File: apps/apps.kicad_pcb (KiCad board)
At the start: 2 copper layers, 25 x 25 mm, 14 parts, among them J1 Conn_OUTPUT, Q1 SS9013, U1 XTR117

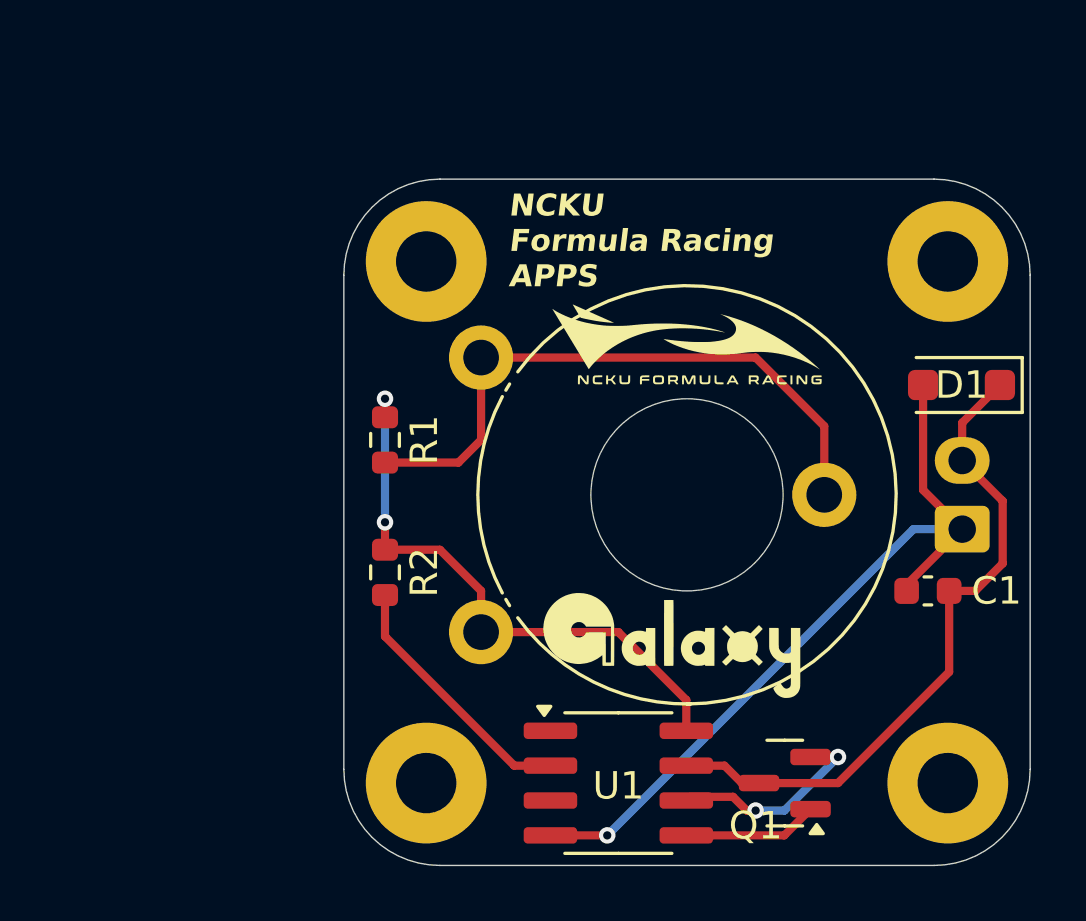
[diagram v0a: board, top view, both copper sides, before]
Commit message: chore: change XTR117 footprint
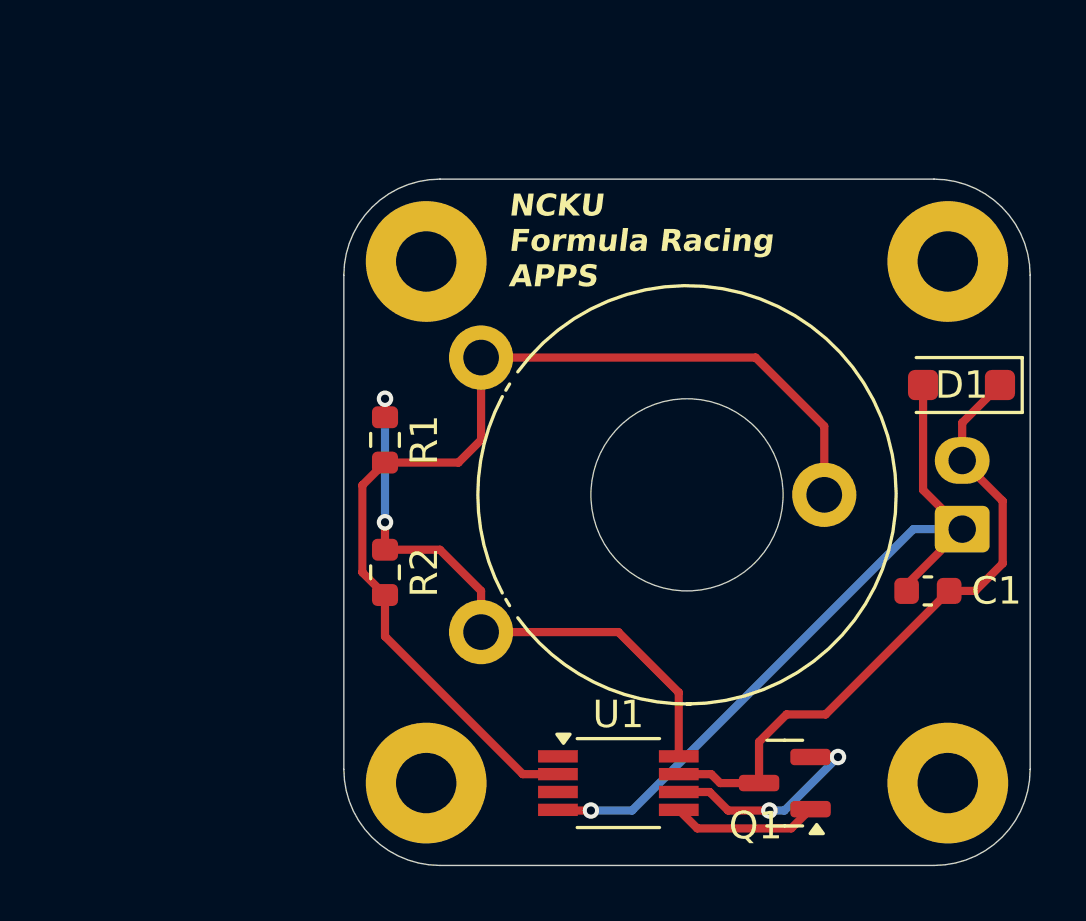
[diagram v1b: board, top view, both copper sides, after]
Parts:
- G*** (x2): moved to B.Cu
- R1: value 83k -> 45k
- RV1: value PT15LV02-253 -> PT15GV02-104
- U1: footprint Package_SO:SOIC-8_3.9x4.9mm_P1.27mm -> Package_SO:VSSOP-8_3.0x3.0mm_P0.65mm
- moved G*** 11.0 mm to (101.5, 53.5), turned to 180 degrees
- moved G*** 4.00 mm to (101.5, 49.5), turned to 180 degrees
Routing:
- net Net-(U1-IIN): track 32.4 -> 38.3 mm
- net Net-(U1-VREG): track 21.4 -> 22.2 mm
- net VDC: track 24.5 -> 23.8 mm
- net Net-(D1-A): track 28.5 -> 27.9 mm
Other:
- board text added: "R=3.5"

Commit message: feat: implement apps pcb
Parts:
- moved D1 11.4 mm to (101.0, 50.5)
- moved G*** 11.4 mm to (91.0, 45.0)
- moved G*** 11.4 mm to (91.0, 49.0)
- moved H1 11.4 mm to (100.5, 46.0)
- moved H2 11.4 mm to (100.5, 65.0)
- moved H3 11.4 mm to (81.5, 65.0)
- moved H4 11.4 mm to (81.5, 46.0)
- moved Q1 11.4 mm to (94.6, 65.0)
- moved R1 11.4 mm to (80.0, 52.5)
- moved R2 11.4 mm to (80.0, 57.3)
- moved U1 11.4 mm to (88.5, 65.0)
- moved J1 11.2 mm to (100.9, 56.8)
- moved RV1 11.1 mm to (83.5, 60.5)
- moved C1 10.5 mm to (99.9, 61.1)
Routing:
- net Net-(Q1-B): track 7.89 -> 10.4 mm
- net Net-(U1-IIN): track 38.3 -> 36.0 mm, vias 0 -> 2
- net Net-(D1-A): track 27.9 -> 26.8 mm, vias 1 -> 0
- net VDC: track 23.8 -> 24.5 mm
- net Net-(U1-VREG): track 22.2 -> 22.8 mm
- net Net-(Q1-E): track 5.37 -> 4.81 mm

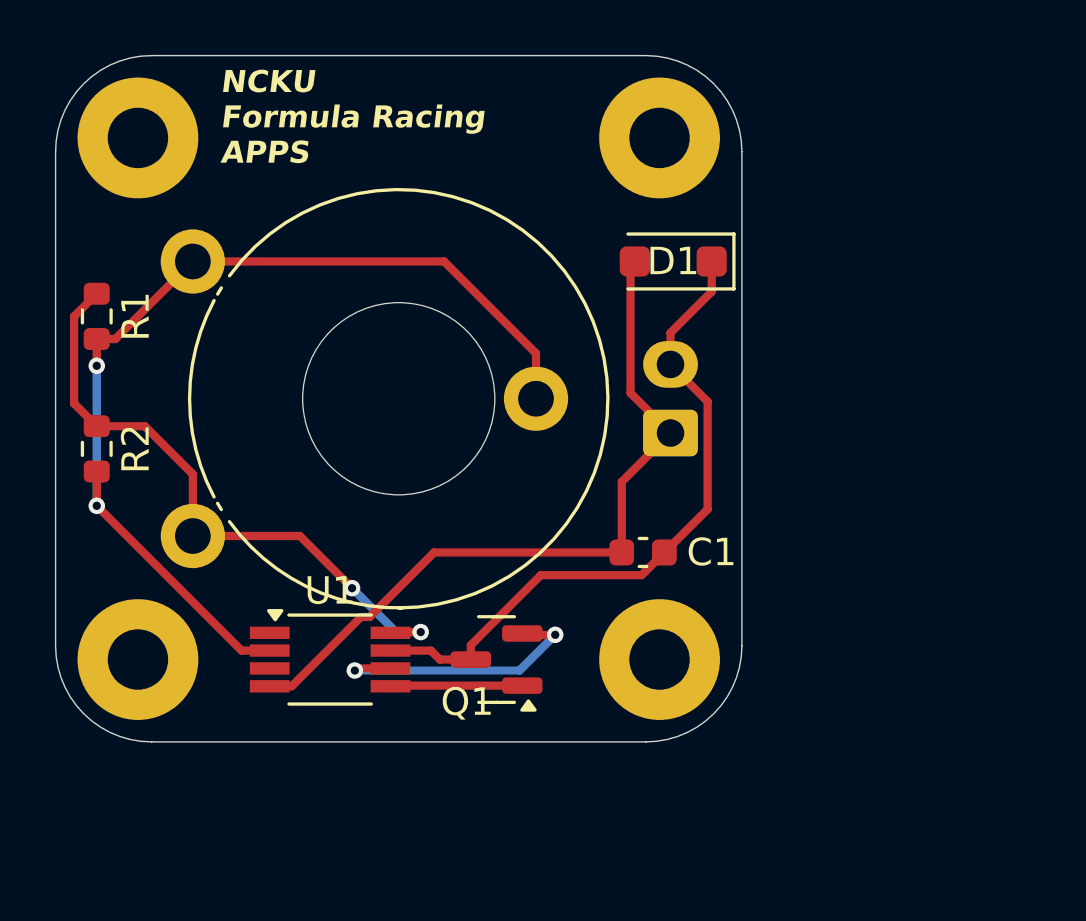
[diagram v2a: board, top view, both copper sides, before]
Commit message: fix: update resistor
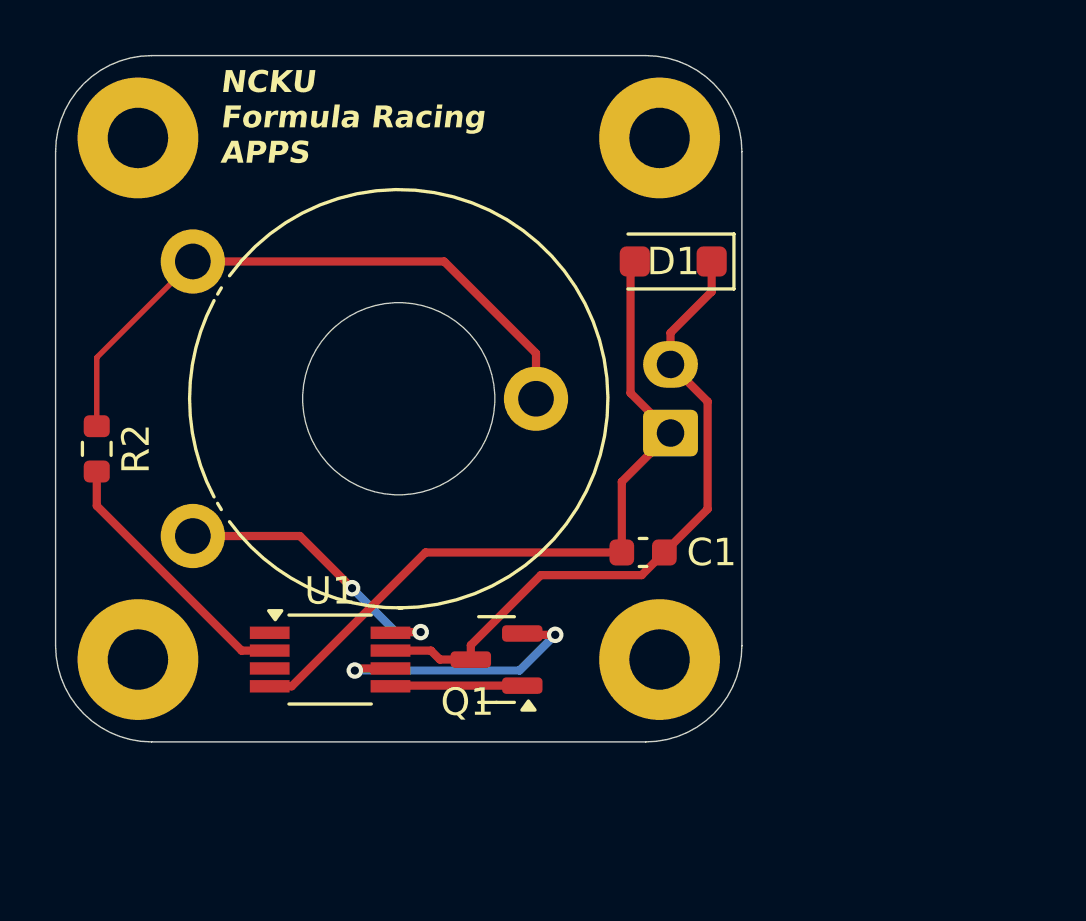
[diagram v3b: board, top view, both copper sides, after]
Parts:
- removed R1: 45k, Resistor_SMD:R_0603_1608Metric
- R2: value 125k -> 25k
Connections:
- R2 pad 1: Net-(U1-VREG) -> Net-(R2-Pad1)
- RV1 pad 2: Net-(U1-IIN) -> Net-(R2-Pad1)
- RV1 pad 3: Net-(U1-IIN) -> Net-(R2-Pad1)
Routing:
- net Net-(U1-IIN): track 36.0 -> 9.73 mm, vias 2 -> 0
- net Net-(R2-Pad1): track 0.00 -> 23.0 mm
- net Net-(U1-VREG): track 22.8 -> 10.9 mm

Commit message: update the version of APPS
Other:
- board text added: "APPS 4mA~20mA Output Rev. 2026.02"
- board text removed: "APPS 4mA~20mA Output Rev. 2025.03"
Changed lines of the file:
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@@
 			(outputformat 1)
 			(mirror no)
-			(drillshape 1)
+			(drillshape 0)
 			(scaleselection 1)
-			(outputdirectory "")
+			(outputdirectory "C:/Users/kevin/Desktop/0225_output/APPS/")
 		)
 	)
@@
 			(size 4.4 4.4)
 			(drill 2.2)
-			(layers "*.Cu" "*.Mask")
+			(layers "*.Cu" "*.Mask" "In1.Cu" "In2.Cu" "In3.Cu" "In4.Cu" "In5.Cu" "In6.Cu"
+				"In7.Cu" "In8.Cu" "In9.Cu" "In10.Cu" "In11.Cu" "In12.Cu" "In13.Cu" "In14.Cu"
+				"In15.Cu" "In16.Cu" "In17.Cu" "In18.Cu" "In19.Cu" "In20.Cu" "In21.Cu"
+				"In22.Cu" "In23.Cu" "In24.Cu" "In25.Cu" "In26.Cu" "In27.Cu" "In28.Cu"
+				"In29.Cu" "In30.Cu"
+			)
 			(remove_unused_layers no)
 			(net 9 "unconnected-(H1-Pad1)")
@@
 			(size 7 7)
 			(drill 7)
-			(layers "*.Cu" "*.Mask")
+			(layers "*.Cu" "*.Mask" "In1.Cu" "In2.Cu" "In3.Cu" "In4.Cu" "In5.Cu" "In6.Cu"
+				"In7.Cu" "In8.Cu" "In9.Cu" "In10.Cu" "In11.Cu" "In12.Cu" "In13.Cu" "In14.Cu"
+				"In15.Cu" "In16.Cu" "In17.Cu" "In18.Cu" "In19.Cu" "In20.Cu" "In21.Cu"
+				"In22.Cu" "In23.Cu" "In24.Cu" "In25.Cu" "In26.Cu" "In27.Cu" "In28.Cu"
+				"In29.Cu" "In30.Cu"
+			)
 		)
 		(pad "1" thru_hole circle
@@
 			(size 2.34 2.34)
 			(drill 1.3)
-			(layers "*.Cu" "*.Mask")
+			(layers "*.Cu" "*.Mask" "In1.Cu" "In2.Cu" "In3.Cu" "In4.Cu" "In5.Cu" "In6.Cu"
+				"In7.Cu" "In8.Cu" "In9.Cu" "In10.Cu" "In11.Cu" "In12.Cu" "In13.Cu" "In14.Cu"
+				"In15.Cu" "In16.Cu" "In17.Cu" "In18.Cu" "In19.Cu" "In20.Cu" "In21.Cu"
+				"In22.Cu" "In23.Cu" "In24.Cu" "In25.Cu" "In26.Cu" "In27.Cu" "In28.Cu"
+				"In29.Cu" "In30.Cu"
+			)
 			(remove_unused_layers no)
 			(net 5 "Net-(U1-VREG)")
@@
 			(size 2.34 2.34)
 			(drill 1.3)
-			(layers "*.Cu" "*.Mask")
+			(layers "*.Cu" "*.Mask" "In1.Cu" "In2.Cu" "In3.Cu" "In4.Cu" "In5.Cu" "In6.Cu"
+				"In7.Cu" "In8.Cu" "In9.Cu" "In10.Cu" "In11.Cu" "In12.Cu" "In13.Cu" "In14.Cu"
+				"In15.Cu" "In16.Cu" "In17.Cu" "In18.Cu" "In19.Cu" "In20.Cu" "In21.Cu"
+				"In22.Cu" "In23.Cu" "In24.Cu" "In25.Cu" "In26.Cu" "In27.Cu" "In28.Cu"
+				"In29.Cu" "In30.Cu"
+			)
 			(remove_unused_layers no)
 			(net 13 "Net-(R2-Pad1)")
@@
 			(size 2.34 2.34)
 			(drill 1.3)
-			(layers "*.Cu" "*.Mask")
+			(layers "*.Cu" "*.Mask" "In1.Cu" "In2.Cu" "In3.Cu" "In4.Cu" "In5.Cu" "In6.Cu"
+				"In7.Cu" "In8.Cu" "In9.Cu" "In10.Cu" "In11.Cu" "In12.Cu" "In13.Cu" "In14.Cu"
+				"In15.Cu" "In16.Cu" "In17.Cu" "In18.Cu" "In19.Cu" "In20.Cu" "In21.Cu"
+				"In22.Cu" "In23.Cu" "In24.Cu" "In25.Cu" "In26.Cu" "In27.Cu" "In28.Cu"
+				"In29.Cu" "In30.Cu"
+			)
 			(remove_unused_layers no)
 			(net 13 "Net-(R2-Pad1)")
@@
 			(size 4.4 4.4)
 			(drill 2.2)
-			(layers "*.Cu" "*.Mask")
+			(layers "*.Cu" "*.Mask" "In1.Cu" "In2.Cu" "In3.Cu" "In4.Cu" "In5.Cu" "In6.Cu"
+				"In7.Cu" "In8.Cu" "In9.Cu" "In10.Cu" "In11.Cu" "In12.Cu" "In13.Cu" "In14.Cu"
+				"In15.Cu" "In16.Cu" "In17.Cu" "In18.Cu" "In19.Cu" "In20.Cu" "In21.Cu"
+				"In22.Cu" "In23.Cu" "In24.Cu" "In25.Cu" "In26.Cu" "In27.Cu" "In28.Cu"
+				"In29.Cu" "In30.Cu"
+			)
 			(remove_unused_layers no)
 			(net 11 "unconnected-(H3-Pad1)")
@@
 			(size 4.4 4.4)
 			(drill 2.2)
-			(layers "*.Cu" "*.Mask")
+			(layers "*.Cu" "*.Mask" "In1.Cu" "In2.Cu" "In3.Cu" "In4.Cu" "In5.Cu" "In6.Cu"
+				"In7.Cu" "In8.Cu" "In9.Cu" "In10.Cu" "In11.Cu" "In12.Cu" "In13.Cu" "In14.Cu"
+				"In15.Cu" "In16.Cu" "In17.Cu" "In18.Cu" "In19.Cu" "In20.Cu" "In21.Cu"
+				"In22.Cu" "In23.Cu" "In24.Cu" "In25.Cu" "In26.Cu" "In27.Cu" "In28.Cu"
+				"In29.Cu" "In30.Cu"
+			)
 			(remove_unused_layers no)
 			(net 10 "unconnected-(H2-Pad1)")
@@
 			(size 4.4 4.4)
 			(drill 2.2)
-			(layers "*.Cu" "*.Mask")
+			(layers "*.Cu" "*.Mask" "In1.Cu" "In2.Cu" "In3.Cu" "In4.Cu" "In5.Cu" "In6.Cu"
+				"In7.Cu" "In8.Cu" "In9.Cu" "In10.Cu" "In11.Cu" "In12.Cu" "In13.Cu" "In14.Cu"
+				"In15.Cu" "In16.Cu" "In17.Cu" "In18.Cu" "In19.Cu" "In20.Cu" "In21.Cu"
+				"In22.Cu" "In23.Cu" "In24.Cu" "In25.Cu" "In26.Cu" "In27.Cu" "In28.Cu"
+				"In29.Cu" "In30.Cu"
+			)
 			(remove_unused_layers no)
 			(net 12 "unconnected-(H4-Pad1)")
@@
 			(size 1.7 2)
 			(drill 1)
-			(layers "*.Cu" "*.Mask")
+			(layers "*.Cu" "*.Mask" "In1.Cu" "In2.Cu" "In3.Cu" "In4.Cu" "In5.Cu" "In6.Cu"
+				"In7.Cu" "In8.Cu" "In9.Cu" "In10.Cu" "In11.Cu" "In12.Cu" "In13.Cu" "In14.Cu"
+				"In15.Cu" "In16.Cu" "In17.Cu" "In18.Cu" "In19.Cu" "In20.Cu" "In21.Cu"
+				"In22.Cu" "In23.Cu" "In24.Cu" "In25.Cu" "In26.Cu" "In27.Cu" "In28.Cu"
+				"In29.Cu" "In30.Cu"
+			)
 			(remove_unused_layers no)
 			(roundrect_rratio 0.147059)
@@
 			(size 1.7 2)
 			(drill 1)
-			(layers "*.Cu" "*.Mask")
+			(layers "*.Cu" "*.Mask" "In1.Cu" "In2.Cu" "In3.Cu" "In4.Cu" "In5.Cu" "In6.Cu"
+				"In7.Cu" "In8.Cu" "In9.Cu" "In10.Cu" "In11.Cu" "In12.Cu" "In13.Cu" "In14.Cu"
+				"In15.Cu" "In16.Cu" "In17.Cu" "In18.Cu" "In19.Cu" "In20.Cu" "In21.Cu"
+				"In22.Cu" "In23.Cu" "In24.Cu" "In25.Cu" "In26.Cu" "In27.Cu" "In28.Cu"
+				"In29.Cu" "In30.Cu"
+			)
 			(remove_unused_layers no)
 			(net 1 "VDC")
@@
 		(layer "User.2")
 	)
-	(gr_text "APPS\n4mA~20mA Output\nRev. 2025.03\n"
+	(gr_text "APPS\n4mA~20mA Output\nRev. 2026.02\n"
 		(at 96.5 67 0)
 		(layer "B.SilkS")
